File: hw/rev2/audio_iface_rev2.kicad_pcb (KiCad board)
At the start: 4 copper layers, 66 x 24.8 mm, 149 parts, among them J1 COAX, J3 USBMICROCONN, J4 CONN_01X02, J6 COAX, J7 COAX, J9 CONN_01X02, P3 CONN_01X06, U2 LTC6242, U3 AK4621, U4 SAM_S70N_TFBGA, U5 TPS61252, U6 LP2992AILD-5.0, U7 LTC6242, U8 TPA6130A2, U9 FAN536xx, X1 7A-16.000MAAJ-T, X2 ASFLM2-12.288MHZ

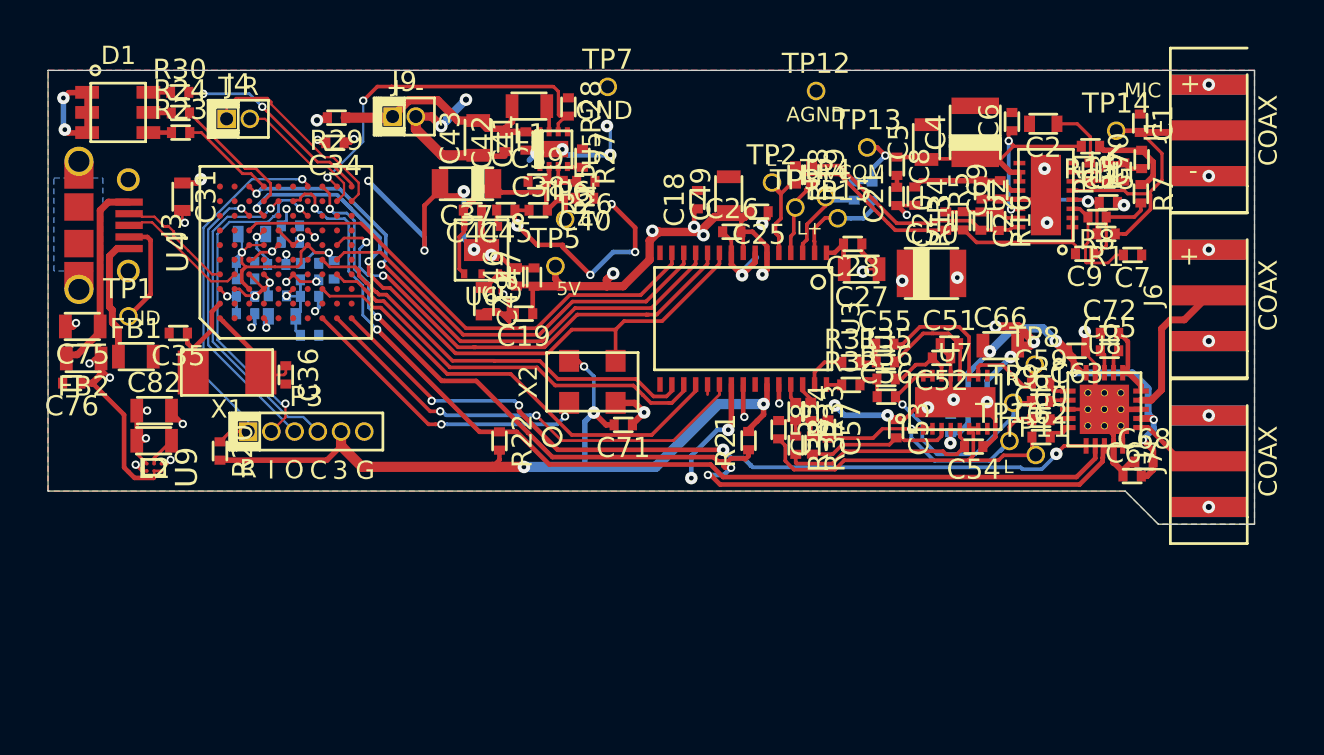
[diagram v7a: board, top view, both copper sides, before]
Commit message: Lots of layout and grounding changes. DRC good
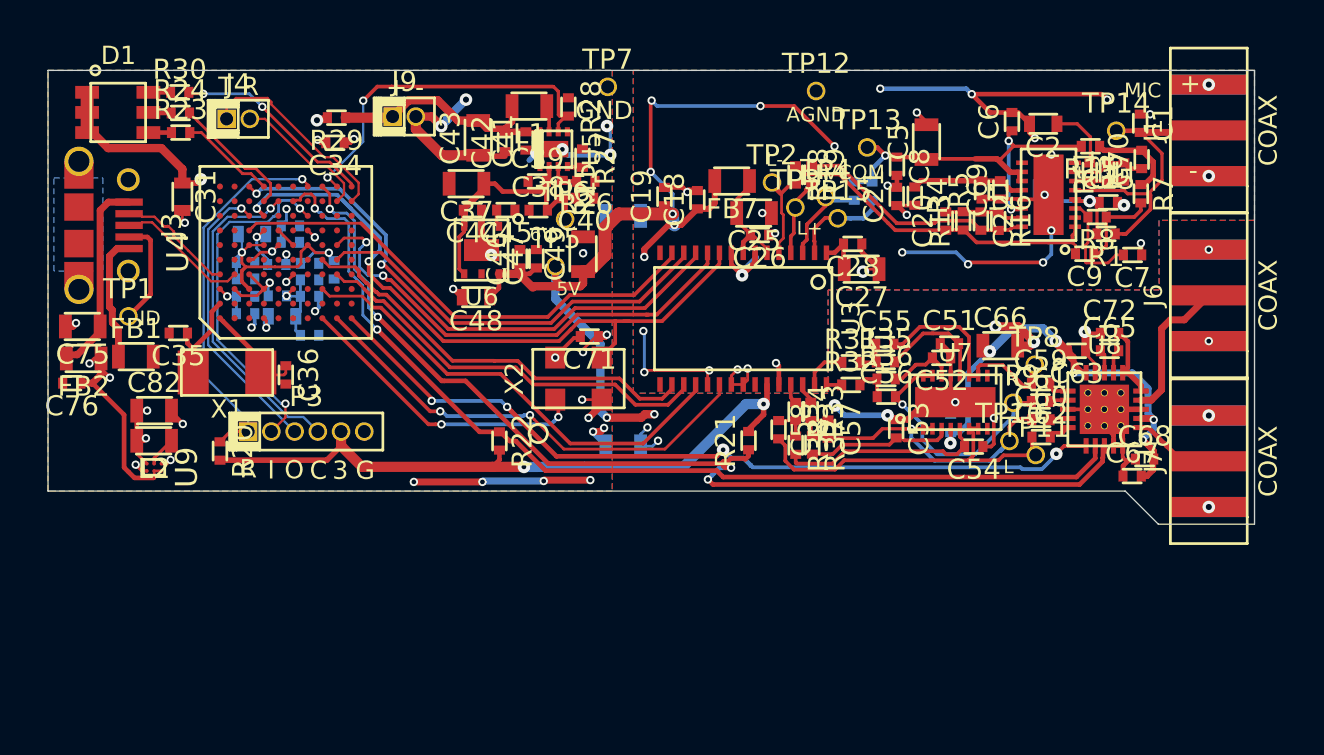
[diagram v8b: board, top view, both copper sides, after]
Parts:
- removed C4, C50: 100u 6.3V, lib:SMD1411_POL
- removed U2: LTC6242, lib:LT_DFN16_QUAD
- added FB5: BLM18PG221SN1D, lib:SMD0805, B.Cu at (183.4, 80.0)
- added FB6: BLM18PG221SN1D, lib:SMD0805, B.Cu at (183.4, 92.5)
- added FB7: BLM18PG221SN1D, lib:SMD0805, F.Cu at (189.4, 78.0)
- added U1: OPAMP_QUAD, lib:LT_DFN16_QUAD, F.Cu at (206.7, 78.8)
- C25: value 1u -> 10u; footprint lib:SMD0402 -> lib:SMD0805
- C37: value 22u -> 10u; footprint lib:SMD1206_POL -> lib:SMD0805
- moved C19 10.0 mm to (185.7, 78.9), turned to 90 degrees
- moved C49 8.62 mm to (181.2, 82.0)
- moved C71 5.17 mm to (181.6, 86.5)
- moved C26 1.53 mm to (190.9, 81.0), turned to 180 degrees
- moved C47 1.01 mm to (178.7, 82.3)
- moved C46 1.01 mm to (177.8, 82.3)
- moved X2 0.78 mm to (181.0, 88.8)
- moved C48 0.48 mm to (175.4, 84.4), turned to 180 degrees
- moved C25 0.28 mm to (190.6, 79.8)
- moved C13 0.22 mm to (206.6, 78.8)
- moved C68 0.16 mm to (211.9, 93.2)
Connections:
- C16 pad 1: AGND_IN -> GND
- C25 pad 2: +5VA -> Net-(C25-Pad2)
- C26 pad 2: +5VA -> Net-(C25-Pad2)
- C29 pad 1: AGND_IN -> GND
- C30 pad 1: AGND_IN -> GND
- C31 pad 1: AGND_IN -> GND
- C32 pad 1: AGND_IN -> GND
- C33 pad 1: AGND_IN -> GND
- C34 pad 1: AGND_IN -> GND
- C35 pad 2: AGND_IN -> GND
- C36 pad 2: AGND_IN -> GND
- C37 pad 2: AGND_IN -> GND
- C38 pad 1: AGND_IN -> GND
- C39 pad 1: AGND_IN -> GND
- C41 pad 1: AGND_IN -> GND
- C42 pad 1: AGND_IN -> GND
- C43 pad 1: AGND_IN -> GND
- C44 pad 1: AGND_IN -> GND
- C45 pad 1: AGND_IN -> GND
- C46 pad 2: AGND_IN -> GND
- C47 pad 2: AGND_IN -> GND
- C48 pad 2: AGND_IN -> GND
- C49 pad 2: AGND_IN -> GND
- C51 pad 1: AGND_IN -> AGND_OUT
- C52 pad 1: AGND_IN -> AGND_OUT
- C53 pad 1: AGND_IN -> AGND_OUT
- C54 pad 1: AGND_IN -> AGND_OUT
- C63 pad 1: AGND_IN -> AGND_OUT
- C64 pad 1: AGND_IN -> AGND_OUT
- C66 pad 2: AGND_IN -> AGND_OUT
- C67 pad 1: AGND_IN -> AGND_OUT
- C68 pad 1: AGND_IN -> AGND_OUT
- C71 pad 1: AGND_IN -> GND
- C72 pad 1: AGND_IN -> AGND_OUT
- C73 pad 1: AGND_IN -> GND
- C74 pad 1: AGND_IN -> GND
- C75 pad 2: AGND_IN -> GND
- C76 pad 2: AGND_IN -> GND
- C77 pad 1: AGND_IN -> GND
- C78 pad 1: AGND_IN -> GND
- C79 pad 1: AGND_IN -> GND
- C80 pad 1: AGND_IN -> GND
- C81 pad 1: AGND_IN -> GND
- C82 pad 2: AGND_IN -> GND
- D1 pad C1: AGND_IN -> GND
- D1 pad C2: AGND_IN -> GND
- D1 pad C3: AGND_IN -> GND
- FB1 pad 2: AGND_IN -> GND
- J6 pad 2: AGND_IN -> AGND_OUT
- J7 pad 2: AGND_IN -> AGND_OUT
- J9 pad 2: AGND_IN -> GND
- P3 pad 6: AGND_IN -> GND
- R26 pad 1: AGND_IN -> GND
- R27 pad 1: AGND_IN -> GND
- R28 pad 1: AGND_IN -> GND
- R39 pad 1: AGND_IN -> GND
- TP7 pad 1: AGND_IN -> GND
- U3 pad 15: (no net) -> Net-(U3-Pad15)
- U3 pad 16: (no net) -> Net-(U3-Pad16)
- U3 pad 24: (no net) -> +5V
- U3 pad 6: +5VA -> Net-(C25-Pad2)
- U3 pad 8: +5VA -> Net-(C25-Pad2)
- U4 pad A10: (no net) -> Net-(U4-PadA10)
- U4 pad A5: (no net) -> Net-(U4-PadA5)
- U4 pad A6: (no net) -> Net-(U4-PadA6)
- U4 pad A7: (no net) -> Net-(U4-PadA7)
- U4 pad A8: AGND_IN -> GND
- U4 pad A9: (no net) -> Net-(U4-PadA9)
- U4 pad B1: (no net) -> Net-(U4-PadB1)
- U4 pad B10: (no net) -> Net-(U4-PadB10)
- U4 pad B2: (no net) -> Net-(U4-PadB2)
- U4 pad B3: AGND_IN -> GND
- U4 pad B5: (no net) -> Net-(U4-PadB5)
- U4 pad B6: (no net) -> Net-(U4-PadB6)
- U4 pad B7: (no net) -> Net-(U4-PadB7)
- U4 pad B8: (no net) -> Net-(U4-PadB8)
- U4 pad B9: (no net) -> Net-(U4-PadB9)
- U4 pad C1: (no net) -> Net-(U4-PadC1)
- U4 pad C2: (no net) -> Net-(U4-PadC2)
- U4 pad C4: AGND_IN -> GND
- U4 pad C9: (no net) -> Net-(U4-PadC9)
- U4 pad D2: (no net) -> Net-(U4-PadD2)
- U4 pad D3: AGND_IN -> GND
- U4 pad D4: AGND_IN -> GND
- U4 pad D5: (no net) -> Net-(U4-PadD5)
- U4 pad E1: (no net) -> Net-(U4-PadE1)
- U4 pad E10: (no net) -> Net-(U4-PadE10)
- U4 pad E2: (no net) -> Net-(U4-PadE2)
- U4 pad E3: (no net) -> Net-(U4-PadE3)
- U4 pad E5: (no net) -> Net-(U4-PadE5)
- U4 pad E7: AGND_IN -> GND
- U4 pad E8: (no net) -> Net-(U4-PadE8)
- U4 pad F1: (no net) -> Net-(U4-PadF1)
- U4 pad F10: (no net) -> Net-(U4-PadF10)
- U4 pad F2: (no net) -> Net-(U4-PadF2)
- U4 pad F4: AGND_IN -> GND
- U4 pad F5: AGND_IN -> GND
- U4 pad F6: AGND_IN -> GND
- U4 pad F7: (no net) -> Net-(U4-PadF7)
- U4 pad F8: (no net) -> Net-(U4-PadF8)
- U4 pad G1: (no net) -> Net-(U4-PadG1)
- U4 pad G2: (no net) -> Net-(U4-PadG2)
- U4 pad G3: (no net) -> Net-(U4-PadG3)
- U4 pad G4: (no net) -> Net-(U4-PadG4)
- U4 pad G5: (no net) -> Net-(U4-PadG5)
- U4 pad G9: (no net) -> Net-(U4-PadG9)
- U4 pad H2: (no net) -> Net-(U4-PadH2)
- U4 pad H4: (no net) -> Net-(U4-PadH4)
- U4 pad H6: (no net) -> Net-(U4-PadH6)
- U4 pad H7: (no net) -> Net-(U4-PadH7)
- U4 pad H8: (no net) -> Net-(U4-PadH8)
- U4 pad H9: (no net) -> Net-(U4-PadH9)
- U4 pad J2: (no net) -> Net-(U4-PadJ2)
- U4 pad J3: (no net) -> Net-(U4-PadJ3)
- U4 pad J7: (no net) -> Net-(U4-PadJ7)
- U4 pad J8: (no net) -> Net-(U4-PadJ8)
- U4 pad K2: (no net) -> Net-(U4-PadK2)
- U4 pad K3: (no net) -> /Microcontroller/SPI1_SIN
- U4 pad K4: (no net) -> Net-(U4-PadK4)
- U4 pad K5: (no net) -> Net-(U4-PadK5)
- U4 pad K6: (no net) -> Net-(U4-PadK6)
- U4 pad K7: (no net) -> Net-(U4-PadK7)
- U4 pad K8: (no net) -> Net-(U4-PadK8)
- U5 pad 1: AGND_IN -> GND
- U5 pad 5: (no net) -> Net-(U5-Pad5)
- U5 pad PAD: AGND_IN -> GND
- U6 pad 2: AGND_IN -> GND
- U6 pad PAD: AGND_IN -> GND
- U7 pad Vss: AGND_IN -> AGND_OUT
- U8 pad 10: AGND_IN -> AGND_OUT
- U8 pad 13: AGND_IN -> AGND_OUT
- U8 pad 19: AGND_IN -> AGND_OUT
- U8 pad 3: AGND_IN -> AGND_OUT
- U8 pad 9: AGND_IN -> AGND_OUT
- U8 pad PAD: AGND_IN -> AGND_OUT
- U9 pad A1: AGND_IN -> GND
- U9 pad C2: AGND_IN -> GND
- X2 pad 2: AGND_IN -> GND
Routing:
- net AGND_IN: track 170.3 -> 62.8 mm, vias 59 -> 28
- net GND: track 0.00 -> 61.9 mm, vias 0 -> 29
- net AGND_OUT: track 0.00 -> 43.5 mm, vias 0 -> 13
- net +5VA: track 93.0 -> 111.8 mm, vias 14 -> 17
- net Net-(C25-Pad2): track 0.00 -> 7.46 mm
- net +3V: track 60.7 -> 61.6 mm, vias 12 -> 11
- net /CODEC/BICK: track 31.8 -> 31.0 mm
- net /Microcontroller/CODEC_SDIN: track 23.2 -> 22.5 mm
- net /Microcontroller/CODEC_SDO: track 27.7 -> 27.0 mm
- net /Microcontroller/CODEC_LRCK: track 27.3 -> 26.6 mm
- net (no net): track 0.00 -> 0.07 mm, vias 0 -> 1
- added copper zone on Inner1.Cu, net +3V
- added copper zone on Inner2.Cu, net AGND_OUT
- added copper zone on B.Cu, net GND
- added copper zone on F.Cu, net GND
- added copper zone on Inner1.Cu, net GND
- added copper zone on Inner2.Cu, net GND
- removed copper zone on Inner2.Cu, net +3V
